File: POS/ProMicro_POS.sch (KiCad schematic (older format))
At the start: 36 parts, among them J1 uFL, J2 Coax, U1 MPU-9250, U2 AP2112K-1.8, U3 SIM28ML

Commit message: update schematic and PCBs
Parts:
- A1, JP1, JP2, JP3, JP4: Config DNP -> (none); Variant (none) -> DNP
- C1, C6: Config -GPS,+GYRO -> (none); MPN (none) -> CL05B103KB5NNNC; Variant (none) -> -GPS,+GYRO; manf# CL05B103KB5NNNC -> (none)
- C10, C11, J1, J2, L1, R1: Config +GPS,-GYRO -> (none); Variant (none) -> +GPS,-GYRO
- C2, C3, C4, C5, C7: Config -GPS,+GYRO -> (none); MPN (none) -> CL05B104KO5NNNC; Variant (none) -> -GPS,+GYRO; manf# CL05B104KO5NNNC -> (none)
- C8: Config +GPS,-GYRO -> (none); MPN (none) -> CL10A475KO8NNNC; Variant (none) -> +GPS,-GYRO; manf# CL10A475KO8NNNC -> (none)
- C9: Config +GPS,-GYRO -> (none); MPN (none) -> CL05B104KO5NNNC; Variant (none) -> +GPS,-GYRO; manf# CL05B104KO5NNNC -> (none)
- D1: Config +GPS,-GYRO -> (none); MPN (none) -> 19-217/BHC-ZL1M2RY/3T; Variant (none) -> +GPS,-GYRO; manf# 19-217/BHC-ZL1M2RY/3T -> (none)
- R2: Config +GPS,-GYRO -> (none); MPN (none) -> 0402WGF0000TCE; Variant (none) -> +GPS,-GYRO; manf# 0402WGF0000TCE -> (none)
- R3: Config +GPS,-GYRO -> (none); MPN (none) -> 0402WGF1001TCE; Variant (none) -> +GPS,-GYRO; manf# 0402WGF1001TCE -> (none)
- R4, R5: Config DNP -> (none); MPN (none) -> 0402WGF4701TCE; Variant (none) -> DNP; manf# 0402WGF4701TCE -> (none)
- U1: Config -GPS,+GYRO,+FULL -> (none); MPN (none) -> MPU-9250; Variant (none) -> -GPS,+GYRO; manf# MPU-9250 -> (none)
- U2: Config -GPS,+GYRO -> (none); Variant (none) -> -GPS,+GYRO
- U3: Config +GPS,-GYRO,+FULL -> (none); MPN (none) -> MAX-8C-0-10; Variant (none) -> +GPS,-GYRO; manf# MAX-8C-0-10 -> (none)
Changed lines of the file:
@@
 F 2 "Inductor_SMD:L_0402_1005Metric" H 4900 5000 50  0001 C CNN
 F 3 "~" H 4900 5000 50  0001 C CNN
-F 4 "+GPS,-GYRO" H 4900 5000 50  0001 C CNN "Config"
+F 4 "+GPS,-GYRO" H 4900 5000 50  0001 C CNN "Variant"
 	1    4900 5000
 	0    -1   -1   0
@@
 F 2 "Resistor_SMD:R_0402_1005Metric" V 3730 6100 50  0001 C CNN
 F 3 "~" H 3800 6100 50  0001 C CNN
-F 4 "0402WGF1001TCE" H 3800 6100 50  0001 C CNN "manf#"
+F 4 "0402WGF1001TCE" H 3800 6100 50  0001 C CNN "MPN"
 F 5 "C11702" H 3800 6100 50  0001 C CNN "LCSC#"
-F 6 "+GPS,-GYRO" H 3800 6100 50  0001 C CNN "Config"
+F 6 "+GPS,-GYRO" H 3800 6100 50  0001 C CNN "Variant"
 	1    3800 6100
 	0    1    1    0
@@
 F 2 "Resistor_SMD:R_0402_1005Metric" V 4030 5000 50  0001 C CNN
 F 3 "~" H 4100 5000 50  0001 C CNN
-F 4 "+GPS,-GYRO" H 4100 5000 50  0001 C CNN "Config"
+F 4 "+GPS,-GYRO" H 4100 5000 50  0001 C CNN "Variant"
 	1    4100 5000
 	0    1    1    0
@@
 F 2 "Resistor_SMD:R_0402_1005Metric" V 4830 5800 50  0001 C CNN
 F 3 "~" H 4900 5800 50  0001 C CNN
-F 4 "0402WGF0000TCE" H 4900 5800 50  0001 C CNN "manf#"
+F 4 "0402WGF0000TCE" H 4900 5800 50  0001 C CNN "MPN"
 F 5 "C17168" H 4900 5800 50  0001 C CNN "LCSC#"
-F 6 "+GPS,-GYRO" H 4900 5800 50  0001 C CNN "Config"
+F 6 "+GPS,-GYRO" H 4900 5800 50  0001 C CNN "Variant"
 	1    4900 5800
 	0    1    1    0
@@
 F 2 "Jumper:SolderJumper-2_P1.3mm_Open_RoundedPad1.0x1.5mm" H 1900 6000 50  0001 C CNN
 F 3 "~" H 1900 6000 50  0001 C CNN
-F 4 "DNP" H 1900 6000 50  0001 C CNN "Config"
+F 4 "DNP" H 1900 6000 50  0001 C CNN "Variant"
 	1    1900 6000
 	1    0    0    -1
@@
 F 2 "LED_SMD:LED_0603_1608Metric" H 4100 6500 50  0001 C CNN
 F 3 "~" H 4100 6500 50  0001 C CNN
-F 4 "19-217/BHC-ZL1M2RY/3T" H 4100 6500 50  0001 C CNN "manf#"
+F 4 "19-217/BHC-ZL1M2RY/3T" H 4100 6500 50  0001 C CNN "MPN"
 F 5 "C72041" H 4100 6500 50  0001 C CNN "LCSC#"
-F 6 "+GPS,-GYRO" H 4100 6500 50  0001 C CNN "Config"
+F 6 "+GPS,-GYRO" H 4100 6500 50  0001 C CNN "Variant"
 	1    4100 6500
 	0    -1   -1   0
@@
 F 2 "Connector_Coaxial:U.FL_Hirose_U.FL-R-SMT-1_Vertical" H 6100 5250 50  0001 C CNN
 F 3 "~" H 6100 5250 50  0001 C CNN
-F 4 "+GPS,-GYRO" H 6100 5250 50  0001 C CNN "Config"
+F 4 "+GPS,-GYRO" H 6100 5250 50  0001 C CNN "Variant"
 	1    6100 5250
 	1    0    0    -1
@@
 F 2 "Connector_Coaxial:SMA_Samtec_SMA-J-P-H-ST-EM1_EdgeMount" H 6100 5800 50  0001 C CNN
 F 3 "~" H 6100 5800 50  0001 C CNN
-F 4 "+GPS,-GYRO" H 6100 5800 50  0001 C CNN "Config"
+F 4 "+GPS,-GYRO" H 6100 5800 50  0001 C CNN "Variant"
 	1    6100 5800
 	1    0    0    -1
@@
 F 2 "Capacitor_SMD:C_0603_1608Metric" H 1438 4150 50  0001 C CNN
 F 3 "~" H 1400 4300 50  0001 C CNN
-F 4 "CL10A475KO8NNNC" H 1400 4300 50  0001 C CNN "manf#"
+F 4 "CL10A475KO8NNNC" H 1400 4300 50  0001 C CNN "MPN"
 F 5 "C19666" H 1400 4300 50  0001 C CNN "LCSC#"
-F 6 "+GPS,-GYRO" H 1400 4300 50  0001 C CNN "Config"
+F 6 "+GPS,-GYRO" H 1400 4300 50  0001 C CNN "Variant"
 	1    1400 4300
 	1    0    0    -1
@@
 F 2 "Capacitor_SMD:C_0402_1005Metric" H 4538 5950 50  0001 C CNN
 F 3 "~" H 4500 6100 50  0001 C CNN
-F 4 "+GPS,-GYRO" H 4500 6100 50  0001 C CNN "Config"
+F 4 "+GPS,-GYRO" H 4500 6100 50  0001 C CNN "Variant"
 	1    4500 6100
 	1    0    0    -1
@@
 F 2 "Capacitor_SMD:C_0402_1005Metric" H 5338 5950 50  0001 C CNN
 F 3 "~" H 5300 6100 50  0001 C CNN
-F 4 "+GPS,-GYRO" H 5300 6100 50  0001 C CNN "Config"
+F 4 "+GPS,-GYRO" H 5300 6100 50  0001 C CNN "Variant"
 	1    5300 6100
 	1    0    0    -1
@@
 F 2 "RF_GPS:ublox_MAX" H 3300 5150 50  0001 C CNN
 F 3 "https://www.u-blox.com/sites/default/files/MAX-8_DataSheet_%28UBX-16000093%29.pdf" H 2900 5800 50  0001 C CNN
-F 4 "MAX-8C-0-10" H 2900 5800 50  0001 C CNN "manf#"
-F 5 "+GPS,-GYRO,+FULL" H 2900 5800 50  0001 C CNN "Config"
+F 4 "MAX-8C-0-10" H 2900 5800 50  0001 C CNN "MPN"
+F 5 "+GPS,-GYRO" H 2900 5800 50  0001 C CNN "Variant"
 	1    2900 5800
 	1    0    0    -1
@@
 F 2 "Capacitor_SMD:C_0402_1005Metric" H 5038 2550 50  0001 C CNN
 F 3 "~" H 5000 2700 50  0001 C CNN
-F 4 "CL05B104KO5NNNC" H 5000 2700 50  0001 C CNN "manf#"
+F 4 "CL05B104KO5NNNC" H 5000 2700 50  0001 C CNN "MPN"
 F 5 "C1525" H 5000 2700 50  0001 C CNN "LCSC#"
-F 6 "-GPS,+GYRO" H 5000 2700 50  0001 C CNN "Config"
+F 6 "-GPS,+GYRO" H 5000 2700 50  0001 C CNN "Variant"
 	1    5000 2700
 	1    0    0    -1
@@
 F 2 "Capacitor_SMD:C_0402_1005Metric" H 5538 2550 50  0001 C CNN
 F 3 "~" H 5500 2700 50  0001 C CNN
-F 4 "CL05B103KB5NNNC" H 5500 2700 50  0001 C CNN "manf#"
+F 4 "CL05B103KB5NNNC" H 5500 2700 50  0001 C CNN "MPN"
 F 5 "C15195" H 5500 2700 50  0001 C CNN "LCSC#"
-F 6 "-GPS,+GYRO" H 5500 2700 50  0001 C CNN "Config"
+F 6 "-GPS,+GYRO" H 5500 2700 50  0001 C CNN "Variant"
 	1    5500 2700
 	1    0    0    -1
@@
 F 2 "Sensor_Motion:InvenSense_QFN-24_3x3mm_P0.4mm" H 4000 1000 50  0001 C CNN
 F 3 "https://store.invensense.com/datasheets/invensense/MPU9250REV1.0.pdf" H 4000 1850 50  0001 C CNN
-F 4 "MPU-9250" H 4000 2000 50  0001 C CNN "manf#"
+F 4 "MPU-9250" H 4000 2000 50  0001 C CNN "MPN"
 F 5 "C71459" H 4000 2000 50  0001 C CNN "LCSC#"
-F 6 "-GPS,+GYRO,+FULL" H 4000 2000 50  0001 C CNN "Config"
+F 6 "-GPS,+GYRO" H 4000 2000 50  0001 C CNN "Variant"
 	1    4000 2000
 	1    0    0    -1
@@
 F 2 "Jumper:SolderJumper-2_P1.3mm_Open_RoundedPad1.0x1.5mm" H 5150 1700 50  0001 C CNN
 F 3 "~" H 5150 1700 50  0001 C CNN
-F 4 "DNP" H 5150 1700 50  0001 C CNN "Config"
-F 5 "DNP" H 5150 1700 50  0001 C CNN "Config"
+F 4 "DNP" H 5150 1700 50  0001 C CNN "Variant"
+F 5 "DNP" H 5150 1700 50  0001 C CNN "Variant"
 	1    5150 1700
 	1    0    0    -1
@@
 F 2 "Jumper:SolderJumper-2_P1.3mm_Open_RoundedPad1.0x1.5mm" H 1850 5400 50  0001 C CNN
 F 3 "~" H 1850 5400 50  0001 C CNN
-F 4 "DNP" H 1850 5400 50  0001 C CNN "Config"
+F 4 "DNP" H 1850 5400 50  0001 C CNN "Variant"
 	1    1850 5400
 	-1   0    0    1
@@
 F 2 "Jumper:SolderJumper-2_P1.3mm_Bridged_RoundedPad1.0x1.5mm" H 1850 5500 50  0001 C CNN
 F 3 "~" H 1850 5500 50  0001 C CNN
-F 4 "DNP" H 1850 5500 50  0001 C CNN "Config"
+F 4 "DNP" H 1850 5500 50  0001 C CNN "Variant"
 	1    1850 5500
 	-1   0    0    1
@@
 F 2 "Capacitor_SMD:C_0402_1005Metric" H 6038 2550 50  0001 C CNN
 F 3 "~" H 6000 2700 50  0001 C CNN
-F 4 "CL05B104KO5NNNC" H 6000 2700 50  0001 C CNN "manf#"
+F 4 "CL05B104KO5NNNC" H 6000 2700 50  0001 C CNN "MPN"
 F 5 "C1525" H 6000 2700 50  0001 C CNN "LCSC#"
-F 6 "-GPS,+GYRO" H 6000 2700 50  0001 C CNN "Config"
+F 6 "-GPS,+GYRO" H 6000 2700 50  0001 C CNN "Variant"
 	1    6000 2700
 	1    0    0    -1
@@
 F 2 "Capacitor_SMD:C_0402_1005Metric" H 6538 2525 50  0001 C CNN
 F 3 "~" H 6500 2675 50  0001 C CNN
-F 4 "CL05B104KO5NNNC" H 6500 2675 50  0001 C CNN "manf#"
+F 4 "CL05B104KO5NNNC" H 6500 2675 50  0001 C CNN "MPN"
 F 5 "C1525" H 6500 2675 50  0001 C CNN "LCSC#"
-F 6 "-GPS,+GYRO" H 6500 2675 50  0001 C CNN "Config"
+F 6 "-GPS,+GYRO" H 6500 2675 50  0001 C CNN "Variant"
 	1    6500 2675
 	1    0    0    -1
@@
 F 2 "Capacitor_SMD:C_0402_1005Metric" H 1938 4150 50  0001 C CNN
 F 3 "~" H 1900 4300 50  0001 C CNN
-F 4 "CL05B104KO5NNNC" H 1900 4300 50  0001 C CNN "manf#"
+F 4 "CL05B104KO5NNNC" H 1900 4300 50  0001 C CNN "MPN"
 F 5 "C1525" H 1900 4300 50  0001 C CNN "LCSC#"
-F 6 "+GPS,-GYRO" H 1900 4300 50  0001 C CNN "Config"
+F 6 "+GPS,-GYRO" H 1900 4300 50  0001 C CNN "Variant"
 	1    1900 4300
 	1    0    0    -1
@@
 F 2 "Capacitor_SMD:C_0402_1005Metric" H 6538 1350 50  0001 C CNN
 F 3 "~" H 6500 1500 50  0001 C CNN
-F 4 "CL05B103KB5NNNC" H 6500 1500 50  0001 C CNN "manf#"
+F 4 "CL05B103KB5NNNC" H 6500 1500 50  0001 C CNN "MPN"
 F 5 "C15195" H 6500 1500 50  0001 C CNN "LCSC#"
-F 6 "-GPS,+GYRO" H 6500 1500 50  0001 C CNN "Config"
+F 6 "-GPS,+GYRO" H 6500 1500 50  0001 C CNN "Variant"
 	1    6500 1500
 	1    0    0    -1
@@
 F 2 "Capacitor_SMD:C_0402_1005Metric" H 1288 2500 50  0001 C CNN
 F 3 "~" H 1250 2650 50  0001 C CNN
-F 4 "CL05B104KO5NNNC" H 1250 2650 50  0001 C CNN "manf#"
+F 4 "CL05B104KO5NNNC" H 1250 2650 50  0001 C CNN "MPN"
 F 5 "C1525" H 1250 2650 50  0001 C CNN "LCSC#"
-F 6 "-GPS,+GYRO" H 1250 2650 50  0001 C CNN "Config"
+F 6 "-GPS,+GYRO" H 1250 2650 50  0001 C CNN "Variant"
 	1    1250 2650
 	1    0    0    -1
@@
 F 2 "Capacitor_SMD:C_0402_1005Metric" H 2288 2500 50  0001 C CNN
 F 3 "~" H 2250 2650 50  0001 C CNN
-F 4 "CL05B104KO5NNNC" H 2250 2650 50  0001 C CNN "manf#"
+F 4 "CL05B104KO5NNNC" H 2250 2650 50  0001 C CNN "MPN"
 F 5 "C1525" H 2250 2650 50  0001 C CNN "LCSC#"
-F 6 "-GPS,+GYRO" H 2250 2650 50  0001 C CNN "Config"
+F 6 "-GPS,+GYRO" H 2250 2650 50  0001 C CNN "Variant"
 	1    2250 2650
 	1    0    0    -1
@@
 F 2 "Package_TO_SOT_SMD:SOT-23-5" H 1750 2725 50  0001 C CNN
 F 3 "https://www.diodes.com/assets/Datasheets/AP2112.pdf" H 1750 2500 50  0001 C CNN
-F 4 "-GPS,+GYRO" H 1750 2400 50  0001 C CNN "Config"
+F 4 "-GPS,+GYRO" H 1750 2400 50  0001 C CNN "Variant"
 	1    1750 2400
 	1    0    0    -1
@@
 F 2 "Module:Sparkfun_Pro_Micro" H 9850 1650 50  0001 L CNN
 F 3 "https://cdn.sparkfun.com/datasheets/Dev/Arduino/Boards/Pro_Micro_v13b.pdf" H 9750 2200 50  0001 C CNN
-F 4 "DNP" H 9750 3000 50  0001 C CNN "Config"
+F 4 "DNP" H 9750 3000 50  0001 C CNN "Variant"
 	1    9750 3000
 	1    0    0    -1
@@
 F 2 "Resistor_SMD:R_0402_1005Metric" V 9430 5500 50  0001 C CNN
 F 3 "~" H 9500 5500 50  0001 C CNN
-F 4 "0402WGF4701TCE" H 9500 5500 50  0001 C CNN "manf#"
+F 4 "0402WGF4701TCE" H 9500 5500 50  0001 C CNN "MPN"
 F 5 "C25900" H 9500 5500 50  0001 C CNN "LCSC#"
-F 6 "DNP" H 9500 5500 50  0001 C CNN "Config"
+F 6 "DNP" H 9500 5500 50  0001 C CNN "Variant"
 	1    9500 5500
 	1    0    0    -1
@@
 F 2 "Resistor_SMD:R_0402_1005Metric" V 8930 5500 50  0001 C CNN
 F 3 "~" H 9000 5500 50  0001 C CNN
-F 4 "0402WGF4701TCE" H 9000 5500 50  0001 C CNN "manf#"
+F 4 "0402WGF4701TCE" H 9000 5500 50  0001 C CNN "MPN"
 F 5 "C25900" H 9000 5500 50  0001 C CNN "LCSC#"
-F 6 "DNP" H 9000 5500 50  0001 C CNN "Config"
+F 6 "DNP" H 9000 5500 50  0001 C CNN "Variant"
 	1    9000 5500
 	1    0    0    -1

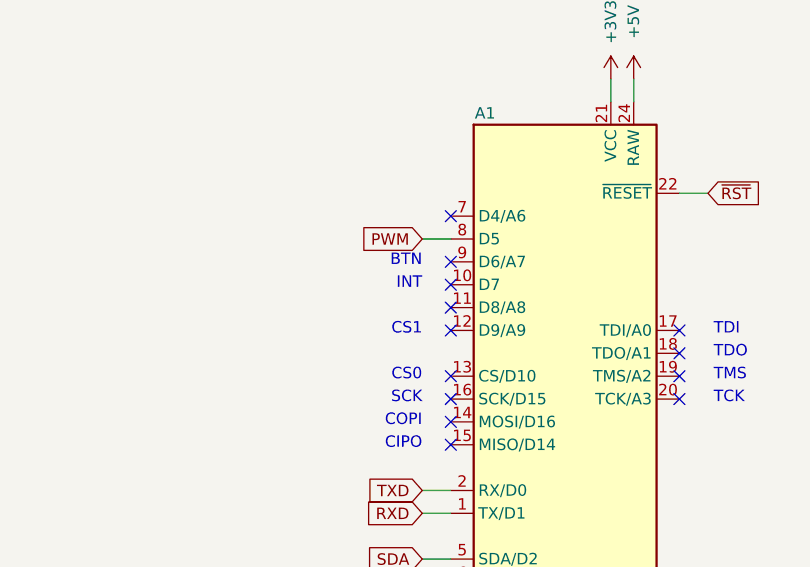
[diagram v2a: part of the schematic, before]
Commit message: fix ERC/DRC and add power planes
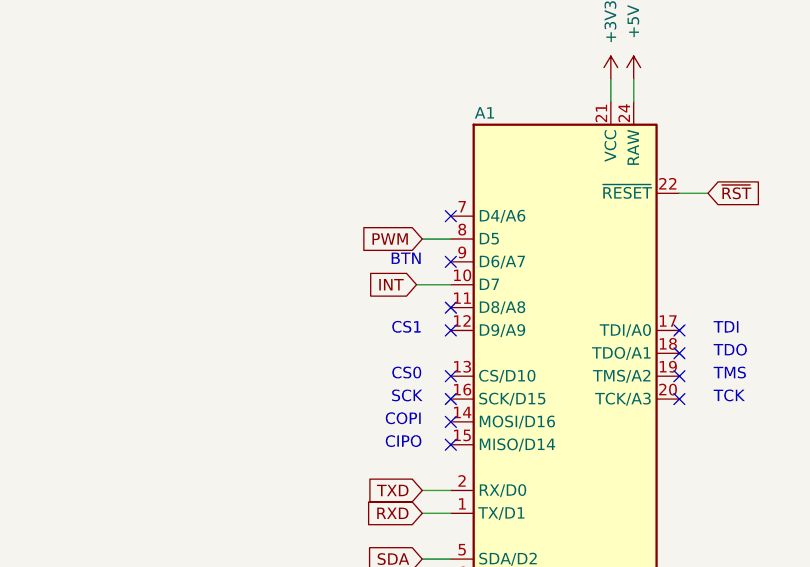
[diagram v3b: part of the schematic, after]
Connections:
- net INT: now also A1.10 (D7)
- no-connect marks 15 -> 14
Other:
- note removed: "INT"
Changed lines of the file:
@@
 Sheet 1 1
 Title "ProMicro_POS"
-Date "2020-10-12"
-Rev "v3.2"
+Date "2020-11-19"
+Rev "v3.3"
 Comp ""
 Comment1 ""
@@
 Text Notes 9125 2525 2    50   ~ 0
 BTN
-Text Notes 9125 2625 2    50   ~ 0
-INT
-NoConn ~ 9250 2600
 NoConn ~ 9250 2500
 $Comp
@@
 	1    0    0    -1
 $EndComp
+Text GLabel 9100 2600 0    50   Input ~ 0
+INT
+Wire Wire Line
+	9100 2600 9250 2600
 $EndSCHEMATC

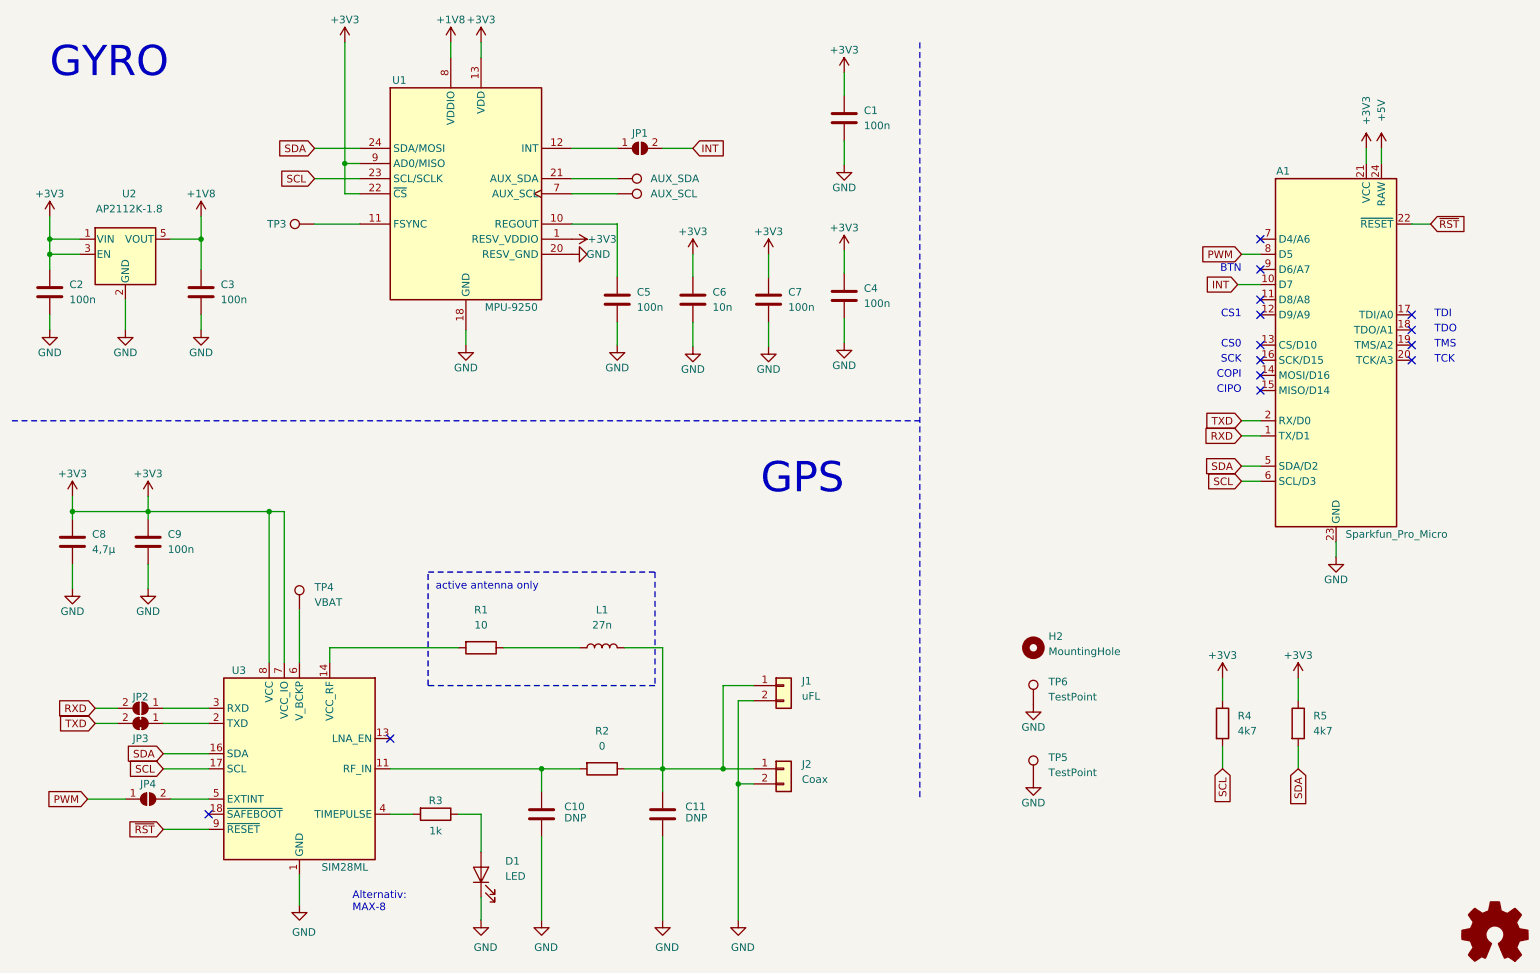
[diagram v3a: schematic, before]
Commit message: made all SMD parts 0603
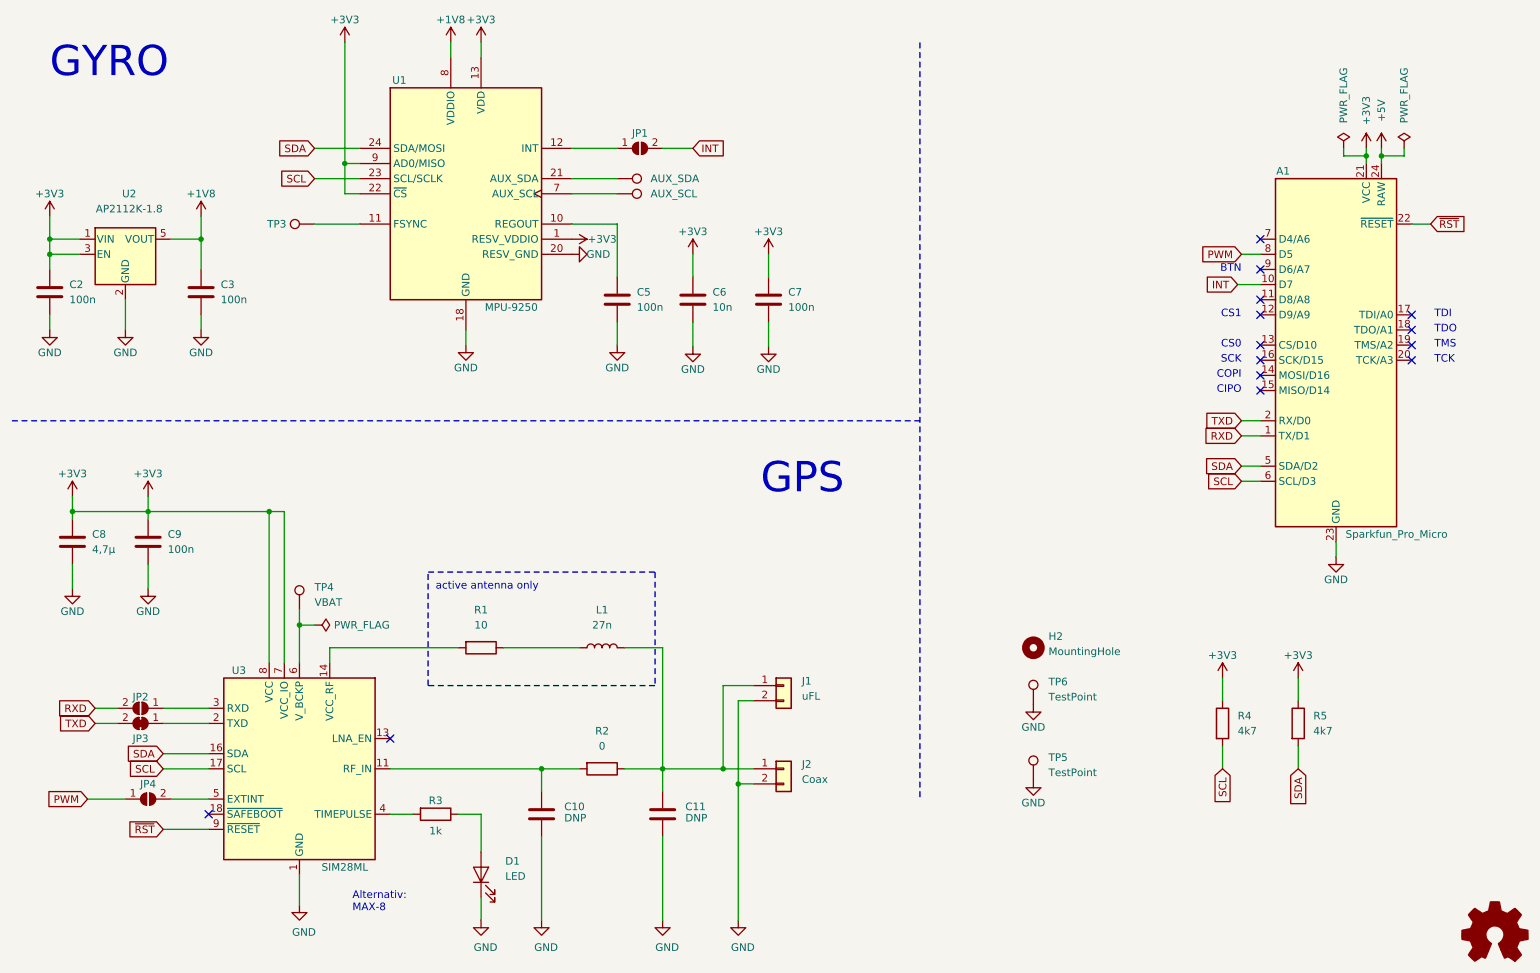
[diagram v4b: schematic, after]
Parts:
- removed C1, C4: 100n, Capacitor_SMD:C_0402_1005Metric, symbol Device:C
- C10, C11, C2, C3, C5, C6, C7, C9: footprint Capacitor_SMD:C_0402_1005Metric -> Capacitor_SMD:C_0603_1608Metric
- L1: footprint Inductor_SMD:L_0402_1005Metric -> Inductor_SMD:L_0603_1608Metric
- R1, R2, R3, R4, R5: footprint Resistor_SMD:R_0402_1005Metric -> Resistor_SMD:R_0603_1608Metric

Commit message: POS
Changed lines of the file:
@@
 NoConn ~ 9250 2800
-Wire Wire Line
-	9950 1700 9950 1750
 Wire Wire Line
 	9000 5200 9000 5350
@@
 F 4 "DNP" H 9750 3000 50  0001 C CNN "Variant"
 	1    9750 3000
-	1    0    0    -1
-$EndComp
-Wire Wire Line
-	10050 1700 10050 1750
-$Comp
-L power:+5V #PWR0103
-U 1 1 5F84FBAC
-P 10050 1700
-F 0 "#PWR0103" H 10050 1550 50  0001 C CNN
-F 1 "+5V" V 10050 1950 50  0000 C CNN
-F 2 "" H 10050 1700 50  0001 C CNN
-F 3 "" H 10050 1700 50  0001 C CNN
-	1    10050 1700
 	1    0    0    -1
 $EndComp
@@
 	9100 2600 9250 2600
 $Comp
-L power:PWR_FLAG #FLG0101
-U 1 1 60033BEE
-P 10200 1700
-F 0 "#FLG0101" H 10200 1775 50  0001 C CNN
-F 1 "PWR_FLAG" V 10200 2050 50  0000 C CNN
-F 2 "" H 10200 1700 50  0001 C CNN
-F 3 "~" H 10200 1700 50  0001 C CNN
-	1    10200 1700
-	1    0    0    -1
-$EndComp
-$Comp
-L power:PWR_FLAG #FLG0102
-U 1 1 600342A4
-P 9800 1700
-F 0 "#FLG0102" H 9800 1775 50  0001 C CNN
-F 1 "PWR_FLAG" V 9800 2050 50  0000 C CNN
-F 2 "" H 9800 1700 50  0001 C CNN
-F 3 "~" H 9800 1700 50  0001 C CNN
-	1    9800 1700
-	1    0    0    -1
-$EndComp
-Wire Wire Line
-	10200 1700 10200 1750
-Wire Wire Line
-	10200 1750 10050 1750
-Connection ~ 10050 1750
-Wire Wire Line
-	10050 1750 10050 1800
-Wire Wire Line
-	9950 1750 9800 1750
-Wire Wire Line
-	9800 1750 9800 1700
-Connection ~ 9950 1750
-Wire Wire Line
-	9950 1750 9950 1800
-$Comp
 L power:PWR_FLAG #FLG0104
 U 1 1 6003F516
@@
 Wire Wire Line
 	9750 4300 9750 4400
+$Comp
+L power:+5V #PWR0103
+U 1 1 5F84FBAC
+P 10050 1700
+F 0 "#PWR0103" H 10050 1550 50  0001 C CNN
+F 1 "+5V" V 10050 1950 50  0000 C CNN
+F 2 "" H 10050 1700 50  0001 C CNN
+F 3 "" H 10050 1700 50  0001 C CNN
+	1    10050 1700
+	1    0    0    -1
+$EndComp
+Wire Wire Line
+	10050 1700 10050 1800
+Wire Wire Line
+	9950 1700 9950 1800
 $EndSCHEMATC
